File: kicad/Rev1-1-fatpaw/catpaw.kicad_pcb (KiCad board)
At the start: 2 copper layers, 79 x 75 mm, 38 parts, among them J1 Conn_01x01_Socket_red, J2 Conn_01x01_Socket_black, J3 m12,Acode,5pin,femalesocket (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, J4 m8, 4Pin Supply Connector FEM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, SW1 1MD1T1B1M6QES, U1 INA826, U2 LM1458mx

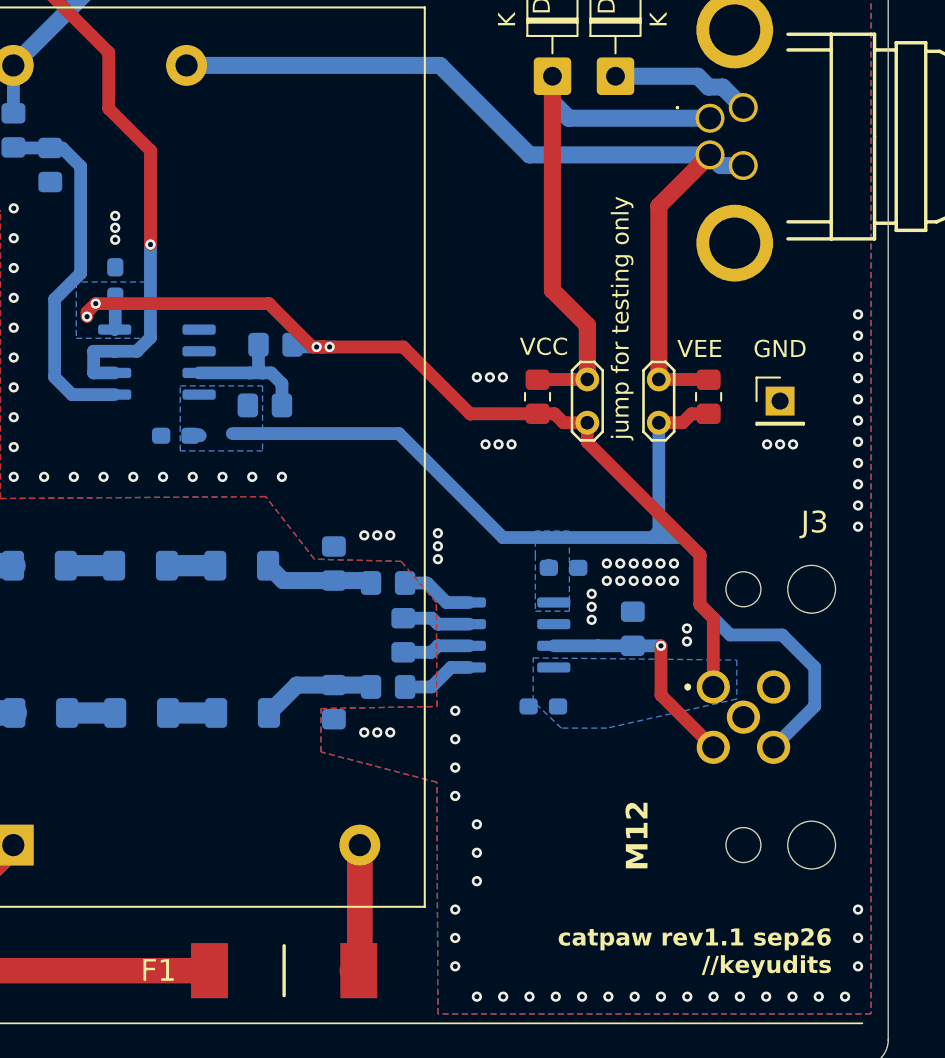
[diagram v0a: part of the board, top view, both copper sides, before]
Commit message: added fatpaw1.1 & catpaw2.0 gerbers
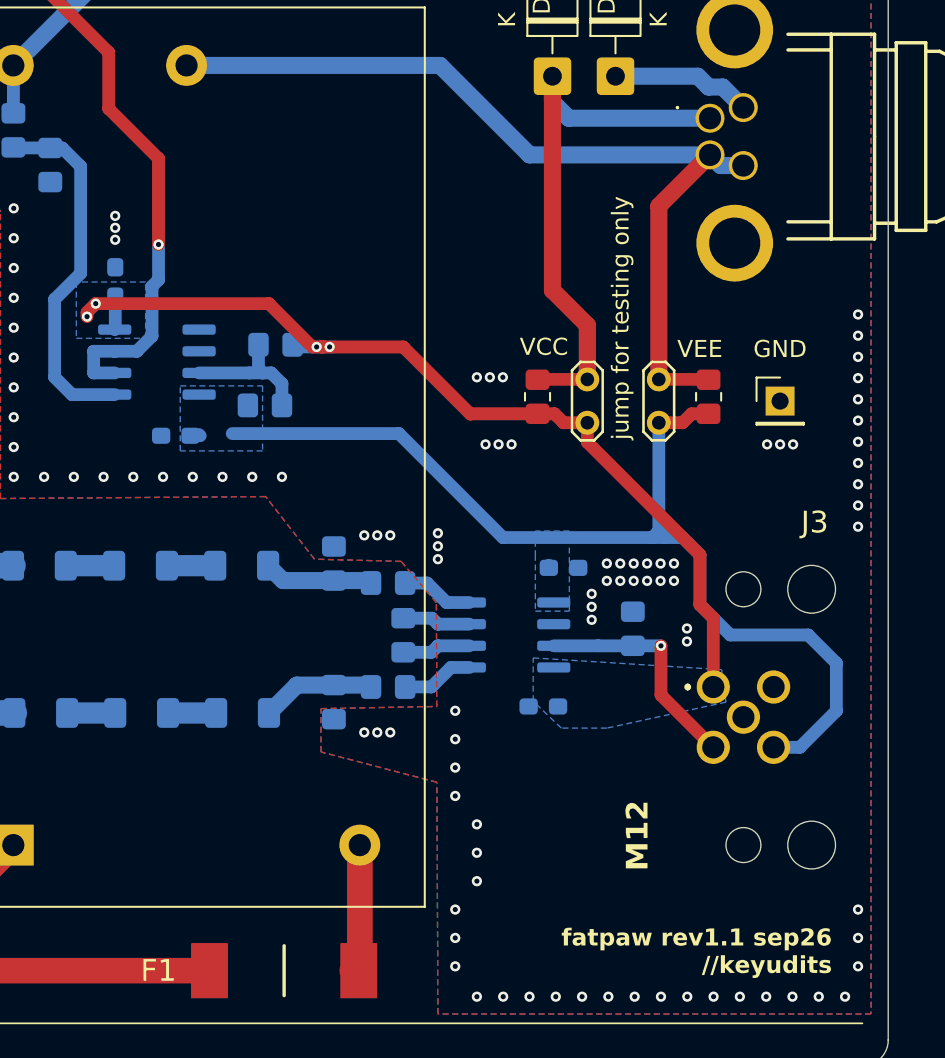
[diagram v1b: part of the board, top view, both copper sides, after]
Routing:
- net /Vcc-: track 58.0 -> 60.9 mm
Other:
- board text added: "fatpaw rev1.1 sep26 //keyudits"
- board text removed: "catpaw rev1.1 sep26 //keyudits"
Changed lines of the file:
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@@
 		(layer "User.2")
 	)
-	(gr_text "catpaw rev1.1 sep26\n//keyudits"
+	(gr_text "fatpaw rev1.1 sep26\n//keyudits"
 		(at 185.42 110.49 0)
 		(layer "F.SilkS")
@@
 	)
 	(segment
+		(start 183.532 97.138)
+		(end 181.99 97.138)
+		(width 0.75)
+		(layer "B.Cu")
+		(net 3)
+	)
+	(segment
+		(start 185.674 92.202)
+		(end 185.674 94.996)
+		(width 0.75)
+		(layer "B.Cu")
+		(net 3)
+	)
+	(segment
 		(start 175.26 78.105)
 		(end 175.26 84.455)
@@
 	)
 	(segment
+		(start 150.245 78.74)
+		(end 160.02 78.74)
+		(width 0.75)
+		(layer "B.Cu")
+		(net 3)
+	)
+	(segment
+		(start 168.8095 86.614)
+		(end 168.8095 86.4605)
+		(width 0.75)
+		(layer "B.Cu")
+		(net 3)
+	)
+	(segment
+		(start 184.023 90.551)
+		(end 185.674 92.202)
+		(width 0.75)
+		(layer "B.Cu")
+		(net 3)
+	)
+	(segment
 		(start 175.641 84.836)
 		(end 176.657 84.836)
@@
 	)
 	(segment
-		(start 150.245 78.74)
-		(end 160.02 78.74)
+		(start 166.116 84.836)
+		(end 174.879 84.836)
 		(width 0.75)
 		(layer "B.Cu")
@@
 	)
 	(segment
-		(start 184.404 92.456)
-		(end 184.404 94.724)
-		(width 0.75)
-		(layer "B.Cu")
-		(net 3)
-	)
-	(segment
-		(start 168.8095 86.614)
-		(end 168.8095 86.4605)
-		(width 0.75)
-		(layer "B.Cu")
-		(net 3)
-	)
-	(segment
-		(start 184.404 94.724)
-		(end 181.99 97.138)
+		(start 177.673 85.852)
+		(end 177.673 88.773)
 		(width 0.75)
 		(layer "B.Cu")
@@
 	)
 	(segment
-		(start 177.673 85.852)
-		(end 177.673 88.773)
-		(width 0.75)
-		(layer "B.Cu")
-		(net 3)
-	)
-	(segment
-		(start 166.116 84.836)
-		(end 174.879 84.836)
-		(width 0.75)
-		(layer "B.Cu")
-		(net 3)
-	)
-	(segment
-		(start 182.499 90.551)
-		(end 184.404 92.456)
-		(width 0.75)
-		(layer "B.Cu")
-		(net 3)
-	)
-	(segment
 		(start 148.303 78.802)
 		(end 148.368 78.867)
@@
 	)
 	(segment
+		(start 179.451 90.551)
+		(end 184.023 90.551)
+		(width 0.75)
+		(layer "B.Cu")
+		(net 3)
+	)
+	(segment
+		(start 185.674 94.996)
+		(end 183.532 97.138)
+		(width 0.75)
+		(layer "B.Cu")
+		(net 3)
+	)
+	(segment
+		(start 160.02 78.74)
+		(end 166.116 84.836)
+		(width 0.75)
+		(layer "B.Cu")
+		(net 3)
+	)
+	(segment
+		(start 174.879 84.836)
+		(end 175.641 84.836)
+		(width 0.75)
+		(layer "B.Cu")
+		(net 3)
+	)
+	(segment
 		(start 176.657 84.836)
 		(end 177.673 85.852)
-		(width 0.75)
-		(layer "B.Cu")
-		(net 3)
-	)
-	(segment
-		(start 160.02 78.74)
-		(end 166.116 84.836)
-		(width 0.75)
-		(layer "B.Cu")
-		(net 3)
-	)
-	(segment
-		(start 174.879 84.836)
-		(end 175.641 84.836)
-		(width 0.75)
-		(layer "B.Cu")
-		(net 3)
-	)
-	(segment
-		(start 179.451 90.551)
-		(end 182.499 90.551)
 		(width 0.75)
 		(layer "B.Cu")
@@
 	)
 	(segment
-		(start 145.452 67.654)
-		(end 145.452 62.14)
+		(start 136.525 49.911)
+		(end 143.002 56.388)
+		(width 0.75)
+		(layer "F.Cu")
+		(net 8)
+	)
+	(segment
+		(start 143.002 59.69)
+		(end 145.923 62.611)
 		(width 0.75)
 		(layer "F.Cu")
@@
 	)
 	(segment
+		(start 145.923 62.611)
+		(end 145.923 67.654)
+		(width 0.75)
+		(layer "F.Cu")
+		(net 8)
+	)
+	(segment
 		(start 115.316 49.911)
 		(end 136.525 49.911)
@@
 		(net 8)
 	)
-	(segment
-		(start 136.525 49.911)
-		(end 143.002 56.388)
-		(width 0.75)
-		(layer "F.Cu")
-		(net 8)
-	)
-	(segment
-		(start 145.452 62.14)
-		(end 143.002 59.69)
-		(width 0.75)
-		(layer "F.Cu")
-		(net 8)
-	)
-	(via
-		(at 145.452 67.654)
+	(via
+		(at 145.923 67.654)
 		(size 0.6)
 		(drill 0.3)
@@
 	)
 	(segment
-		(start 145.452 67.654)
-		(end 145.452 73.115)
+		(start 143.353 73.914)
+		(end 144.653 73.914)
 		(width 0.75)
 		(layer "B.Cu")
@@
 	)
 	(segment
-		(start 144.653 73.914)
-		(end 143.353 73.914)
-		(width 0.75)
-		(layer "B.Cu")
-		(net 8)
-	)
-	(segment
-		(start 145.452 73.115)
-		(end 144.653 73.914)
+		(start 145.542 73.025)
+		(end 145.542 70.104)
 		(width 0.75)
 		(layer "B.Cu")
@@
 	)
 	(segment
+		(start 145.542 70.104)
+		(end 145.923 69.723)
+		(width 0.75)
+		(layer "B.Cu")
+		(net 8)
+	)
+	(segment
+		(start 145.923 69.723)
+		(end 145.923 67.654)
+		(width 0.75)
+		(layer "B.Cu")
+		(net 8)
+	)
+	(segment
 		(start 143.353 73.914)
 		(end 142.117 73.914)
+		(width 0.75)
+		(layer "B.Cu")
+		(net 8)
+	)
+	(segment
+		(start 144.653 73.914)
+		(end 145.542 73.025)
 		(width 0.75)
 		(layer "B.Cu")
@@
 		(polygon
 			(pts
-				(xy 167.89321 91.8953) (xy 179.83121 92.0223) (xy 179.83121 94.3083) (xy 172.212 96.012) (xy 169.545 96.012)
+				(xy 167.89321 91.8953) (xy 178.943 92.583) (xy 179.197 94.488) (xy 172.212 96.012) (xy 169.545 96.012)
 				(xy 167.89321 94.4353)
 			)
@@
 		(polygon
 			(pts
-				(xy 170.0145 84.455) (xy 168.021 84.455) (xy 168.021 85.852) (xy 168.021 85.852) (xy 168.021 89.154)
-				(xy 170.0145 89.154)
+				(xy 170.0145 84.455) (xy 168.021 84.455) (xy 168.021 85.852) (xy 168.021 89.154) (xy 170.0145 89.154)
 			)
 		)
